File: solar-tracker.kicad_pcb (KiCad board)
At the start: 2 copper layers, 135.9 x 47 mm, 29 parts, among them J1 LDR1, J2 LDR2, J3 Motor, J4 Power_9V, J5 FWD_Limit, J6 REV_Limit, Q1 TIP41C, Q2 TIP41C, Q3 TIP42C, Q4 TIP42C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

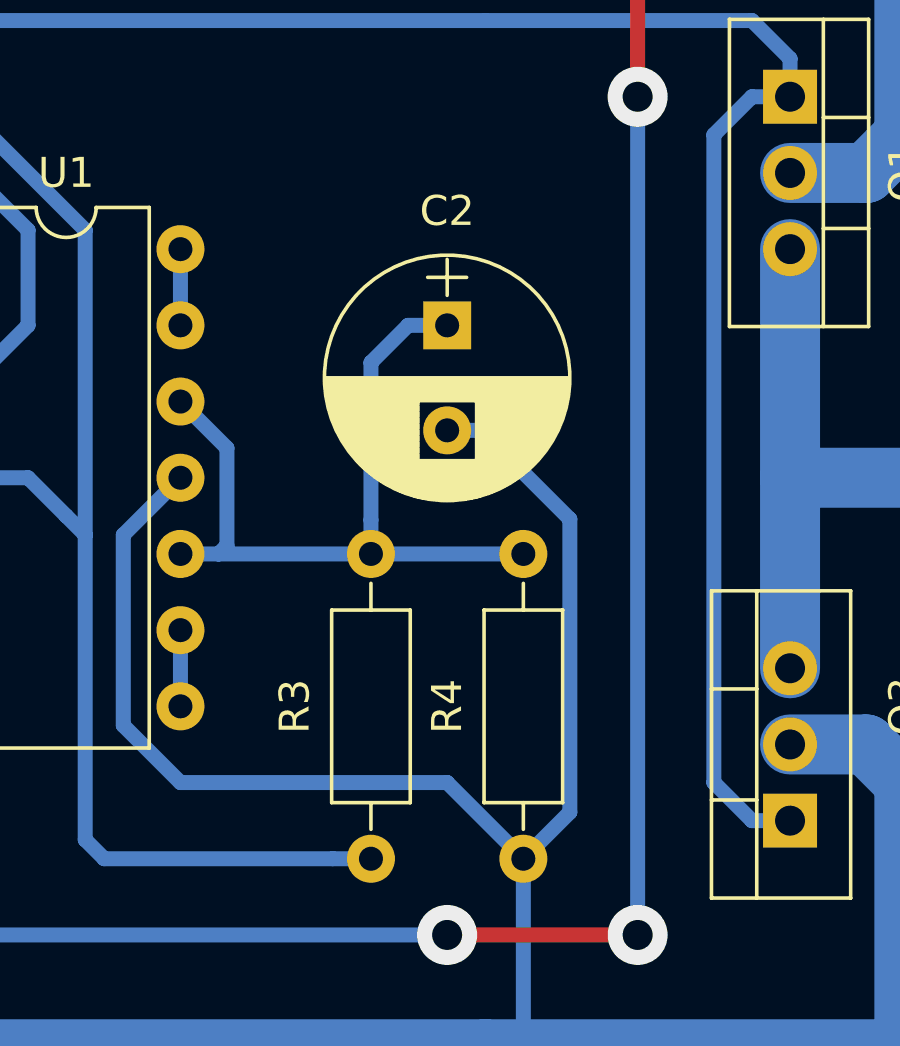
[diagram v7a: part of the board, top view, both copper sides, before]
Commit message: Remove electrolytic capacitor
It's slowing really slow, preventing to measure final voltage on unused
OPAMPs terminals.

Signed-off-by: Sam Protsenko <joe.skb7@gmail.com>
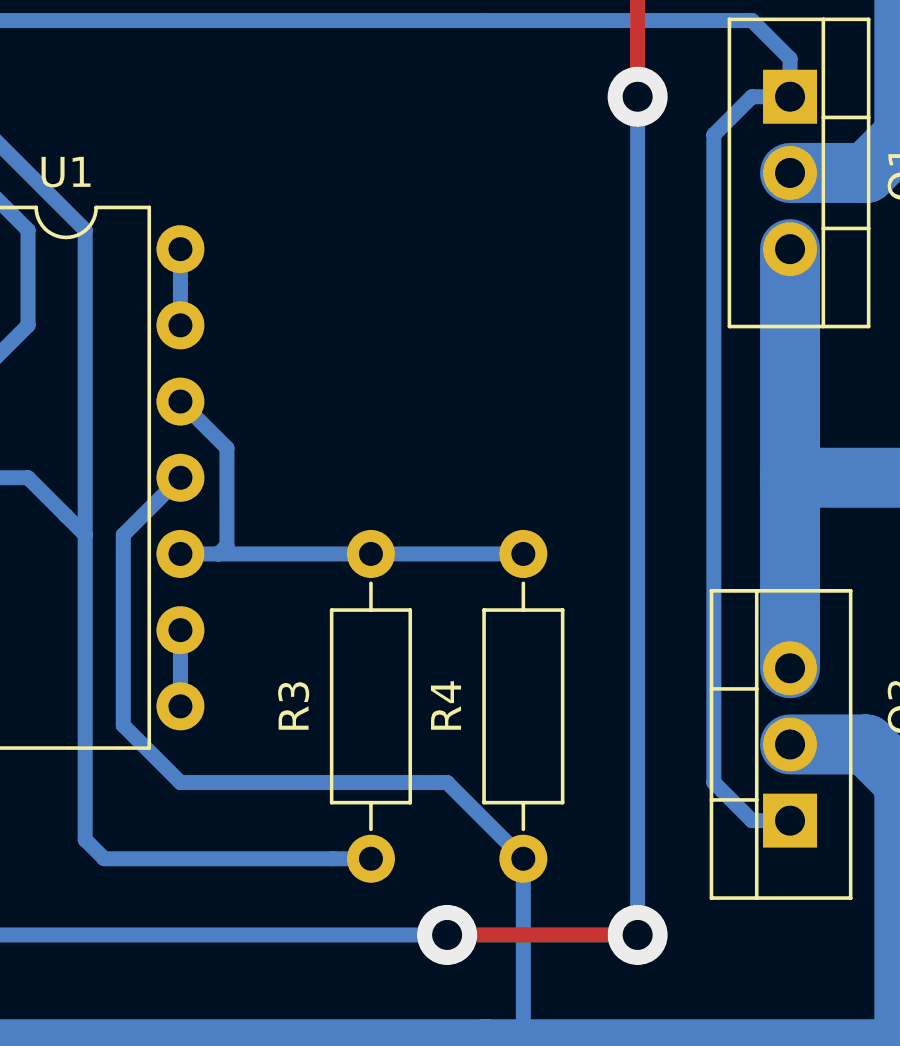
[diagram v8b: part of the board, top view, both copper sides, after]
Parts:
- removed C2: 22uF, Capacitors_THT:CP_Radial_D8.0mm_P3.50mm
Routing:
- net GND: track 238.4 -> 221.2 mm
- net Net-(R3-Pad2): track 26.7 -> 17.3 mm
